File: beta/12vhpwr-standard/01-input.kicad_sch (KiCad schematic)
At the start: 12 parts, among them J2 CEC_FAN_3P (DNP), J3 12V-2x6 IN, Q1 AO3400A

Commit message: Audit BETA electrical and pour pipeline
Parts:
- Q1: Manufacturer AOS -> Alpha & Omega Semiconductor
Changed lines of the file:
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@@
 		(property "Footprint" "cec-Package_TO_SOT_SMD:SOT-23-3_L2.9-W1.3-P1.90-LS2.4-BR" (at 149.86 49.53 0) (effects (font (size 1.27 1.27)) (hide yes)))
 		(property "Datasheet" "https://www.aosmd.com/res/datasheets/AO3400A.pdf" (at 149.86 49.53 0) (effects (font (size 1.27 1.27)) (hide yes)))
-		(property "Manufacturer" "AOS" (at 149.86 49.53 0) (effects (font (size 1.27 1.27)) (hide yes)))
+		(property "Manufacturer" "Alpha & Omega Semiconductor" (at 149.86 49.53 0) (effects (font (size 1.27 1.27)) (hide yes)))
 		(property "MPN" "AO3400A" (at 149.86 49.53 0) (effects (font (size 1.27 1.27)) (hide yes)))
 		(property "LCSC" "C20917" (at 149.86 49.53 0) (effects (font (size 1.27 1.27)) (hide yes)))

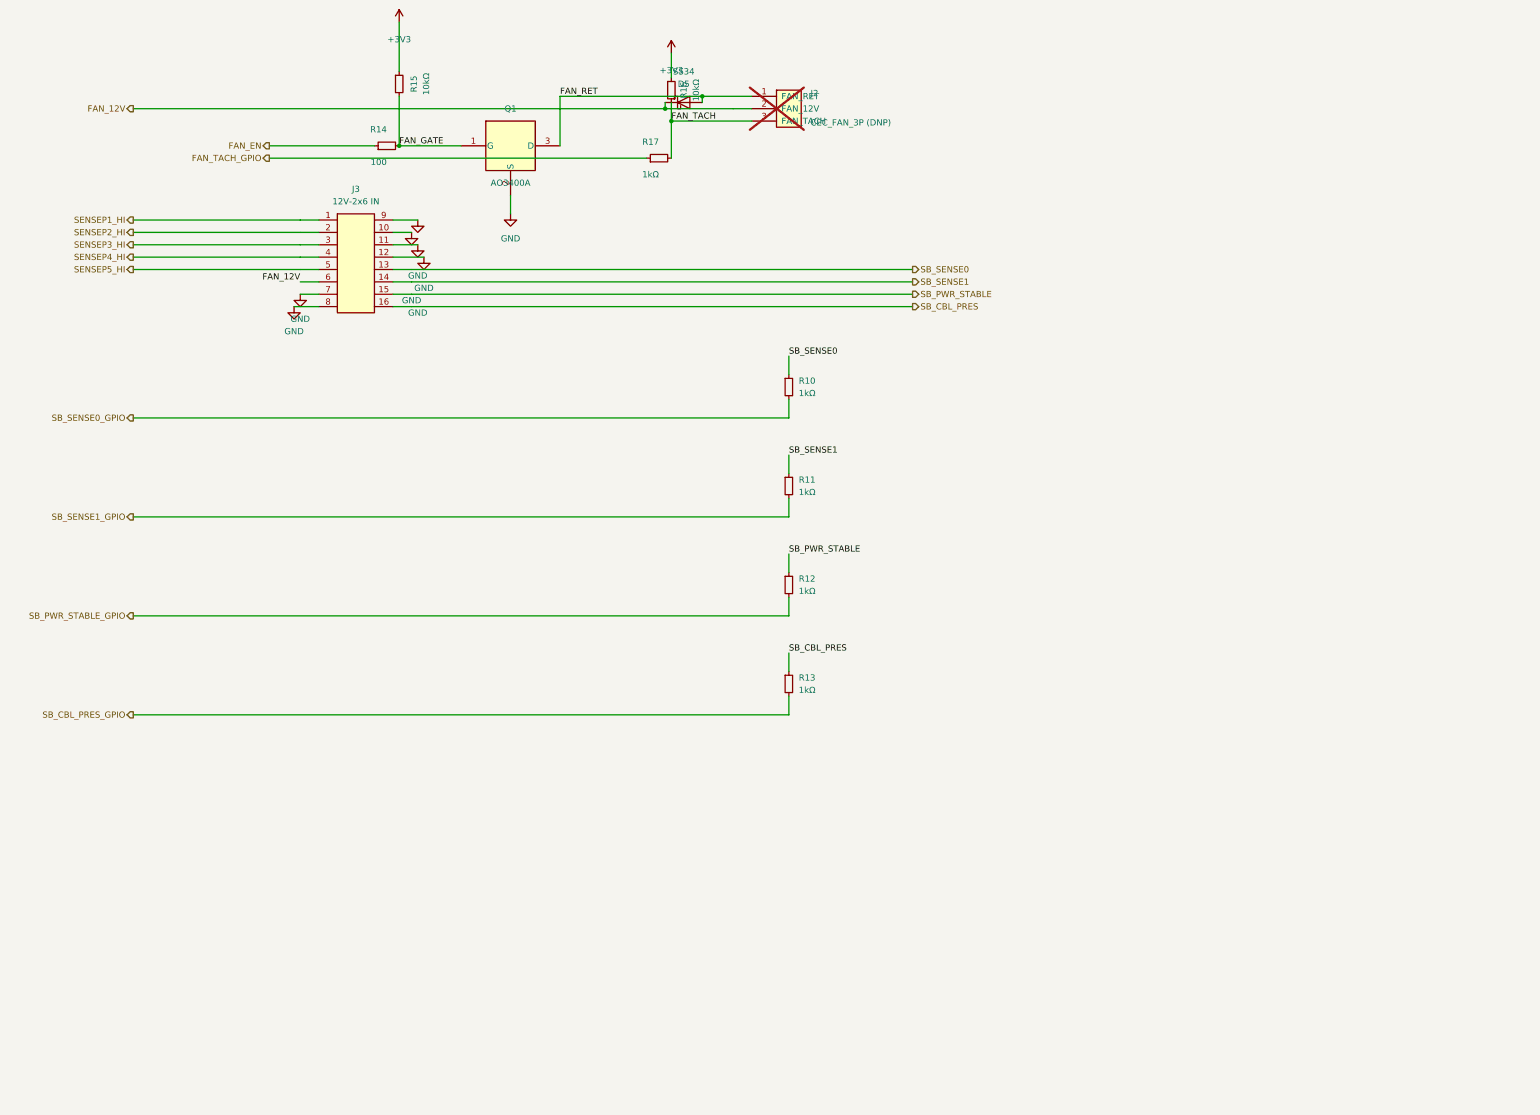
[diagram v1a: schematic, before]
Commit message: Audit BETA power designs and harden PCB pipeline
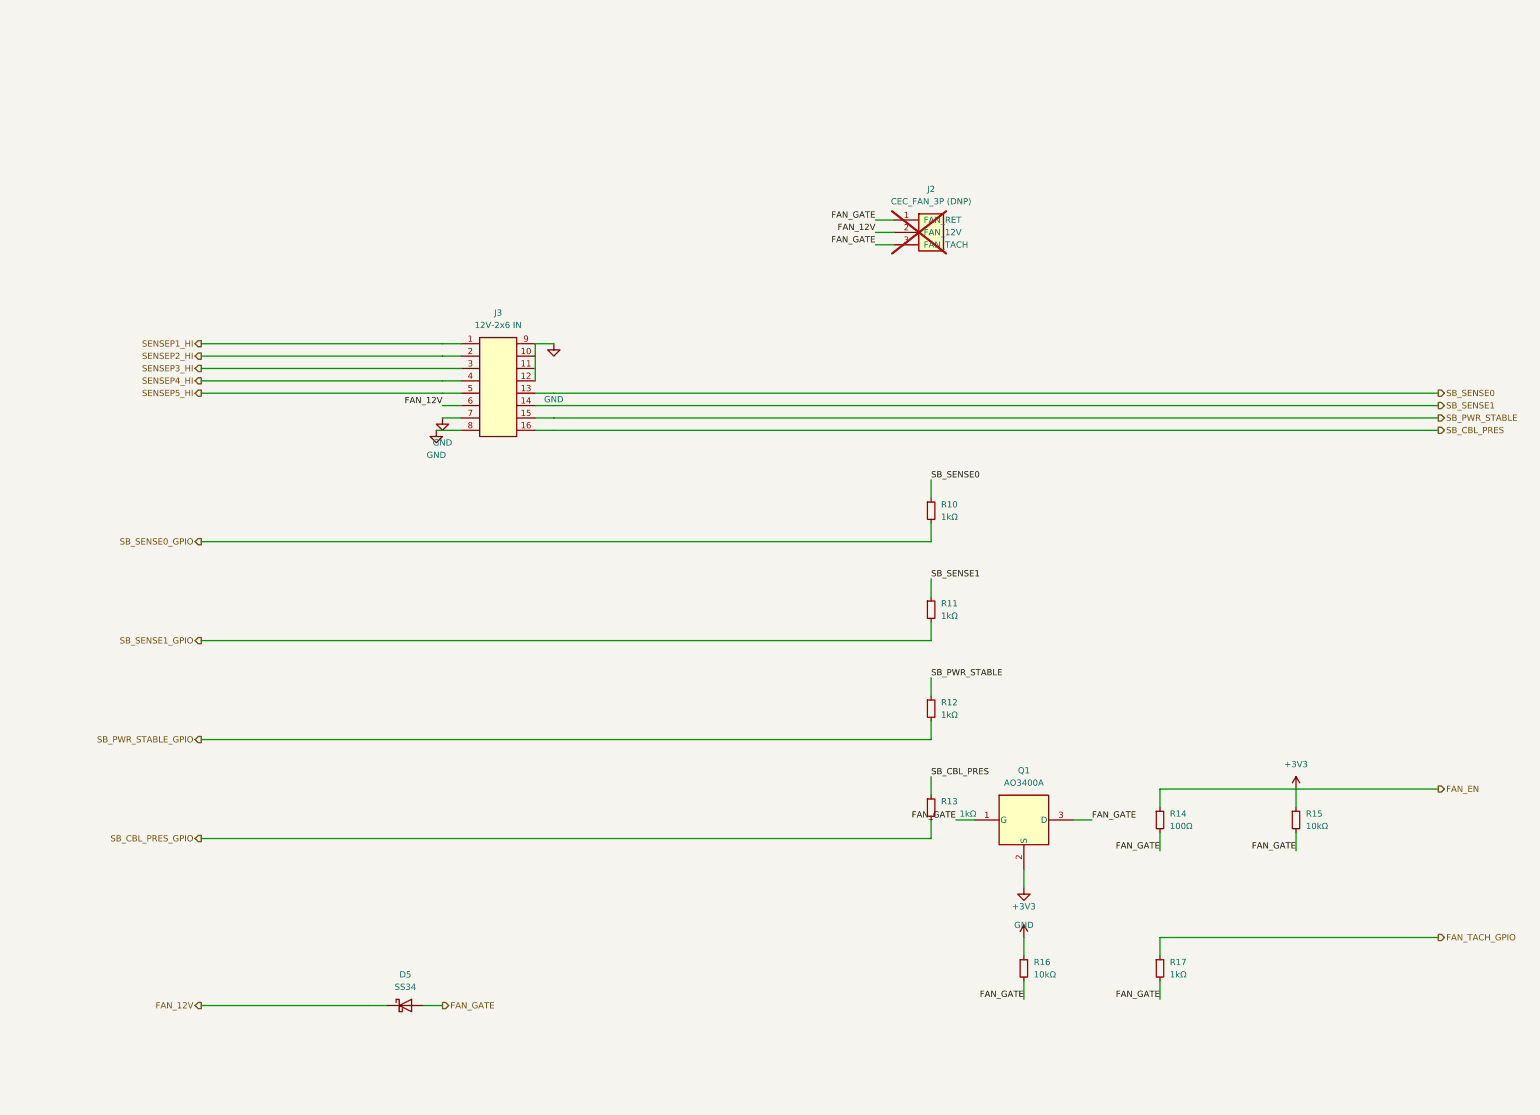
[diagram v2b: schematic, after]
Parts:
- R14: value 100 -> 100Ω
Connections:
- net FAN_RET is gone; now on net FAN_GATE: D5.2 (A), J2.1 (FAN_RET), Q1.3 (D)
- net FAN_TACH is gone; now on net FAN_GATE: J2.3 (FAN_TACH), R16.2, R17.2

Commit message: Rework BETA power rails and schematic composition
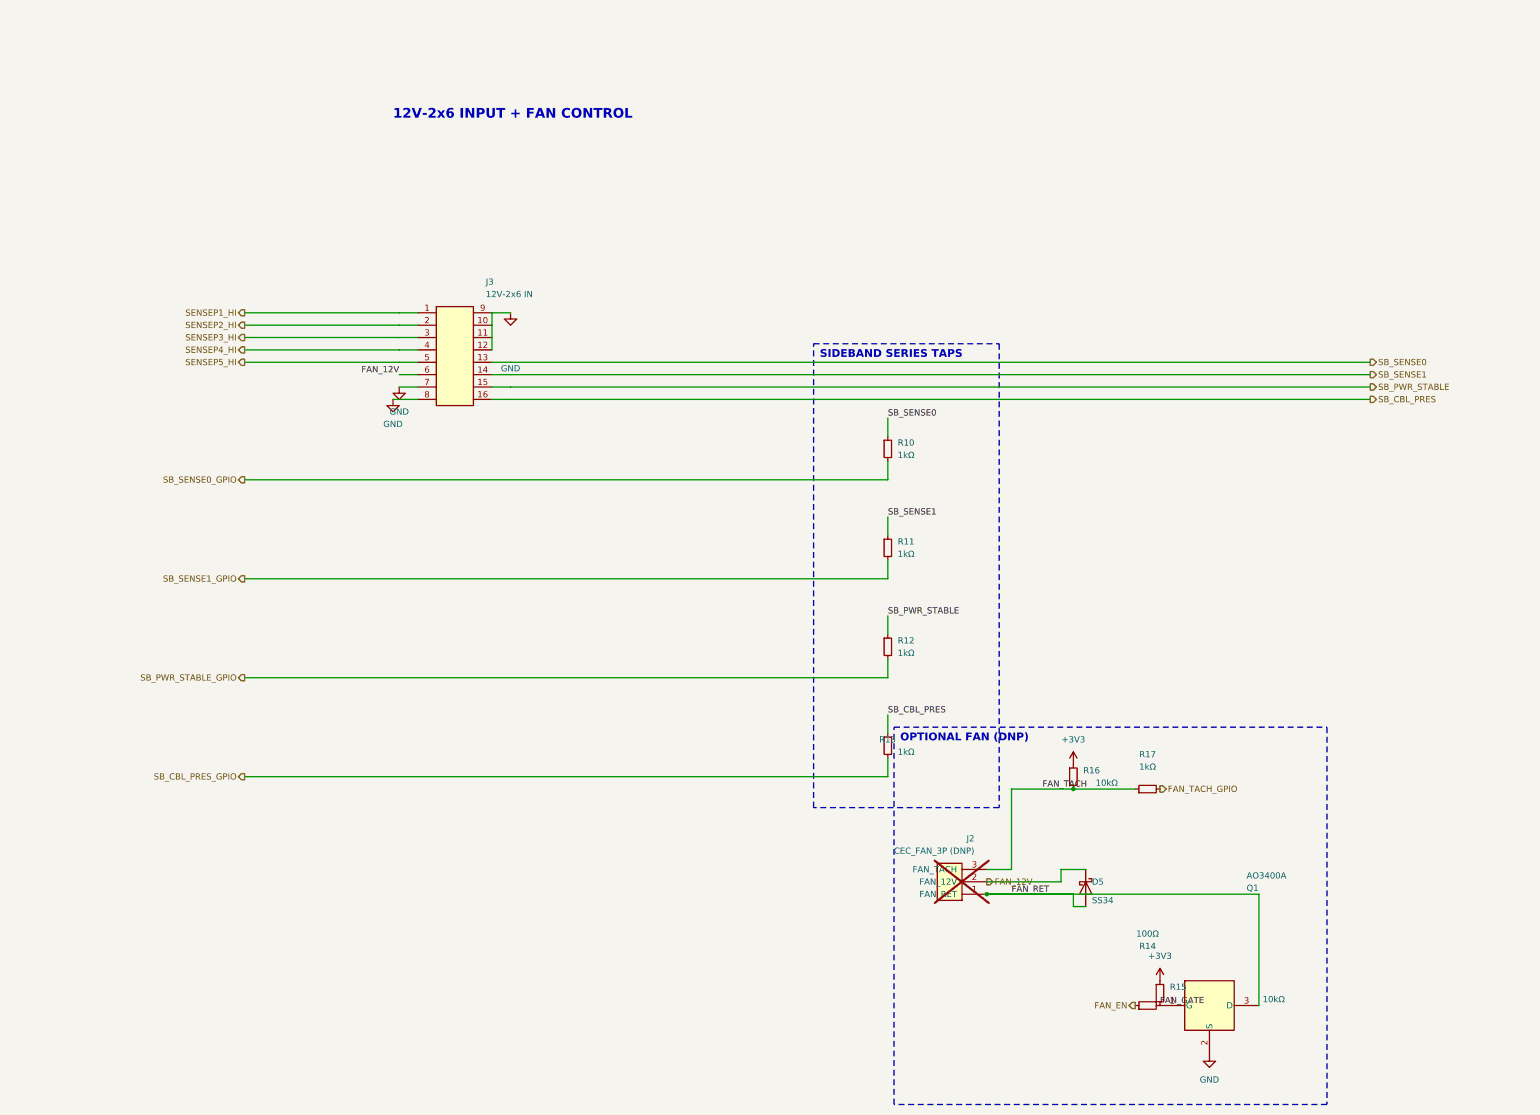
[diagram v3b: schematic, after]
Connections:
- net FAN_GATE: no longer D5.2 (A), J2.1 (FAN_RET), J2.3 (FAN_TACH), Q1.3 (D), R16.2, R17.2
- net FAN_TACH_GPIO: now also R17.2; no longer R17.1
- new net FAN_RET: D5.2 (A), J2.1 (FAN_RET), Q1.3 (D)
- new net FAN_TACH: J2.3 (FAN_TACH), R16.2, R17.1
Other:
- note added: "12V-2x6 INPUT + FAN CONTROL"
- note added: "OPTIONAL FAN (DNP)"
- note added: "SIDEBAND SERIES TAPS"
